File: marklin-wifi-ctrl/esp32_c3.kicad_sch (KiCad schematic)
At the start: 12 parts, among them SW400 RESET, SW401 BOOT, U400 ESP32-C3-MINI-1-N4

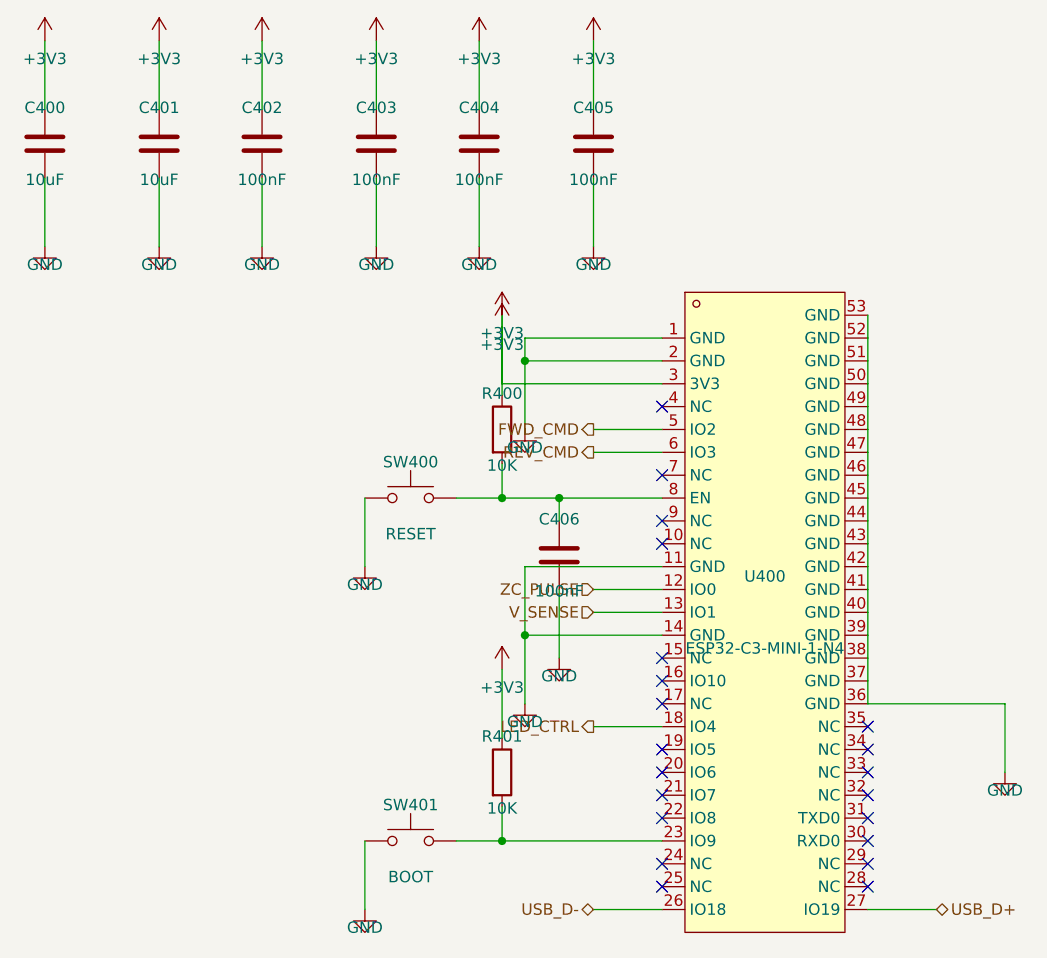
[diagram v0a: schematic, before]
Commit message: Fix ESP32-C3 pin 3 disconnection: overlapping +3V3 power stubs
Pin 3 (3V3) and R400 pull-up had +3V3 stubs at the same x column (100.33).
KiCad GUI merges overlapping collinear wires, losing intermediate endpoints,
causing pin 3 and #PWR0404 to become disconnected. kicad-cli ERC doesn't
detect this because it reads raw wire coordinates before merging.

Fix: move pin 3's +3V3 to x=110.49 (lx - STUB) to avoid overlap.
Added "no overlapping collinear wires" rule to CLAUDE.md and SKILL.md.

Co-Authored-By: Claude Opus 4.6 <noreply@anthropic.com>
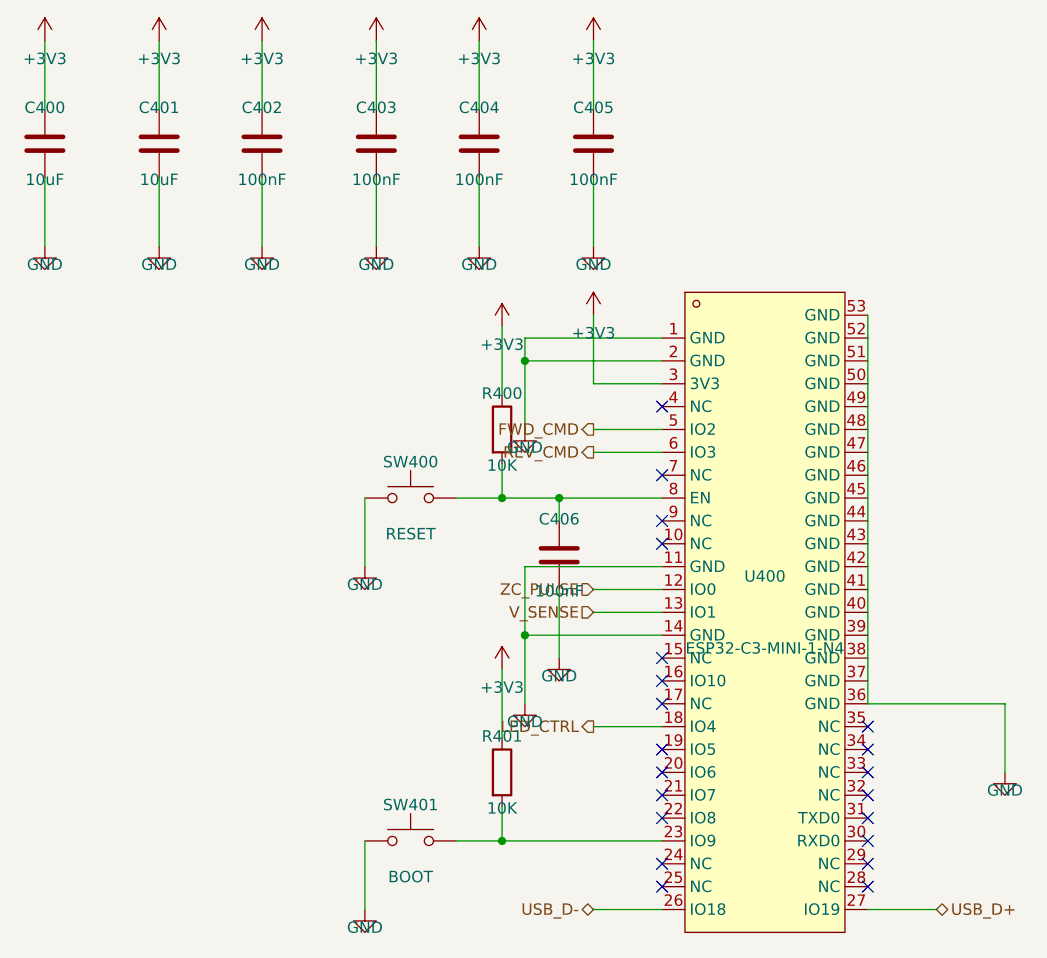
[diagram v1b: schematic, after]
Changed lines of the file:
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@@
 	)
 	(wire
-		(pts (xy 118.11 64.77) (xy 100.33 64.77))
+		(pts (xy 118.11 64.77) (xy 110.49 64.77))
 		(stroke (width 0) (type solid))
 	)
 	(wire
-		(pts (xy 100.33 64.77) (xy 100.33 57.15))
+		(pts (xy 110.49 64.77) (xy 110.49 57.15))
 		(stroke (width 0) (type solid))
 	)
 	(symbol
 		(lib_id "power:+3V3")
-		(at 100.33 57.15 0)
+		(at 110.49 57.15 0)
 		(unit 1)
 		(exclude_from_sim no)
@@
 		(dnp no)
 		(property "Reference" "#PWR0402"
-			(at 100.33 55.15 0)
+			(at 110.49 55.15 0)
 			(effects (font (size 1.27 1.27)) (hide yes))
 		)
 		(property "Value" "+3V3"
-			(at 100.33 59.15 0)
+			(at 110.49 59.15 0)
 			(effects (font (size 1.27 1.27)))
 		)
 		(property "Footprint" ""
-			(at 100.33 57.15 0)
+			(at 110.49 57.15 0)
 			(effects (font (size 1.27 1.27)) (hide yes))
 		)
 		(property "Datasheet" ""
-			(at 100.33 57.15 0)
+			(at 110.49 57.15 0)
 			(effects (font (size 1.27 1.27)) (hide yes))
 		)
